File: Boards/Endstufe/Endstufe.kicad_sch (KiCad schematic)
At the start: 59 parts, among them J1 HV In, J10 240V VU, J2 Relais, J3 Audio_In, J4 Übertrager, J5 Gegenkopplung, J6 12V out, J7 Conn_01x08, J8 12V In, J9 VU-Meter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

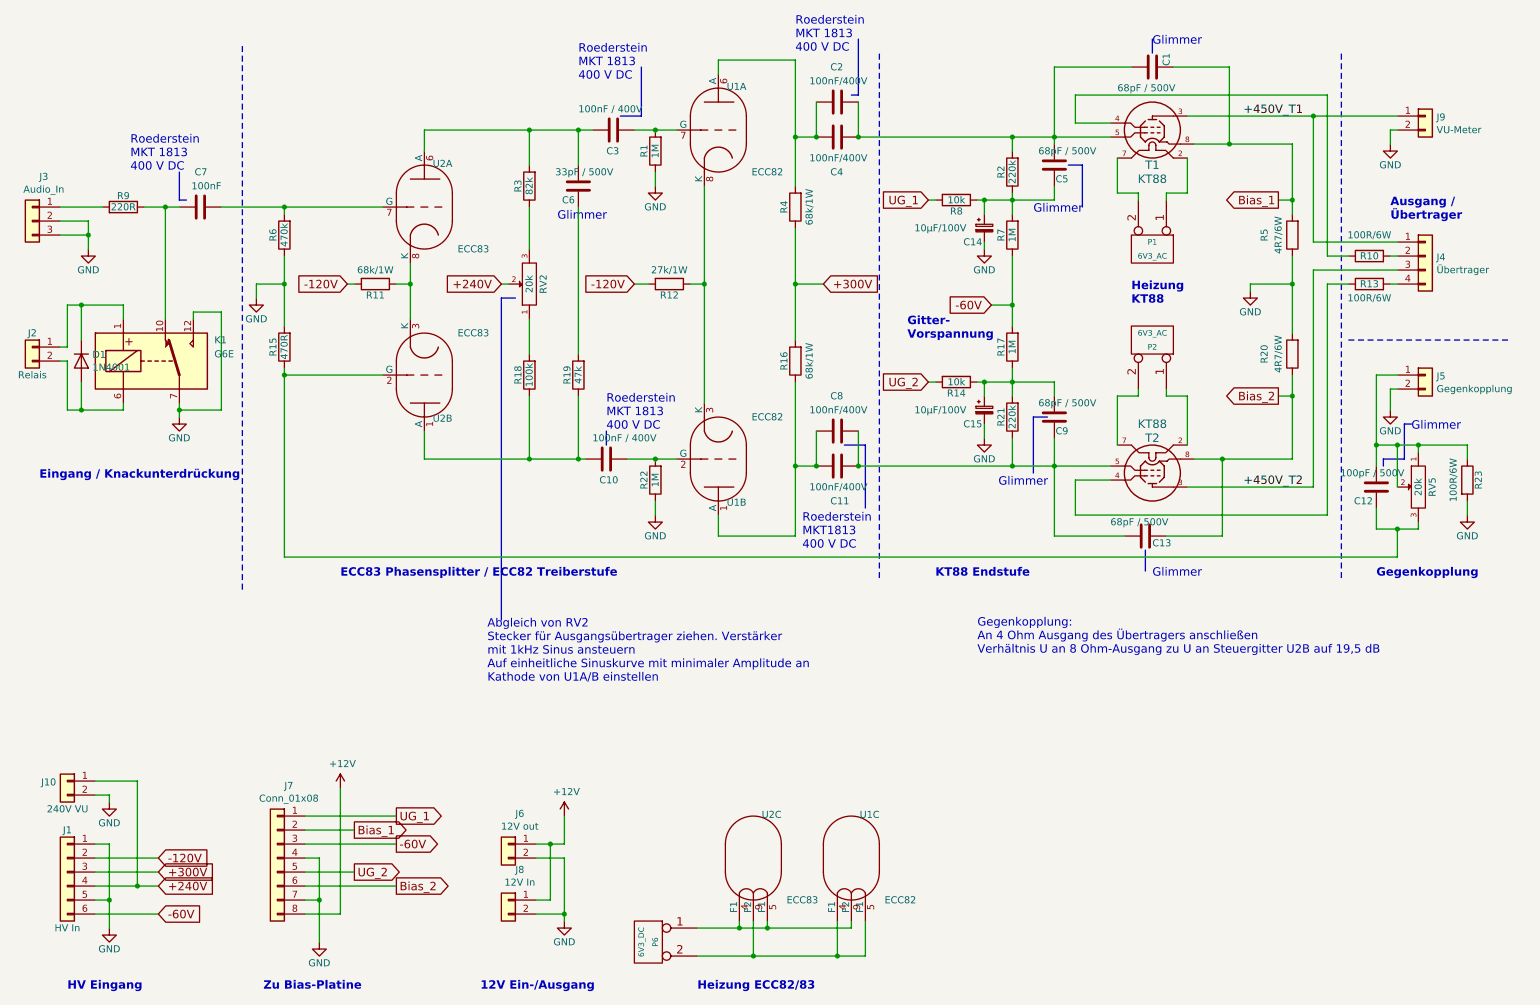
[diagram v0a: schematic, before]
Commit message: 6.3V, 400V und 400V Regler Boards bestellt
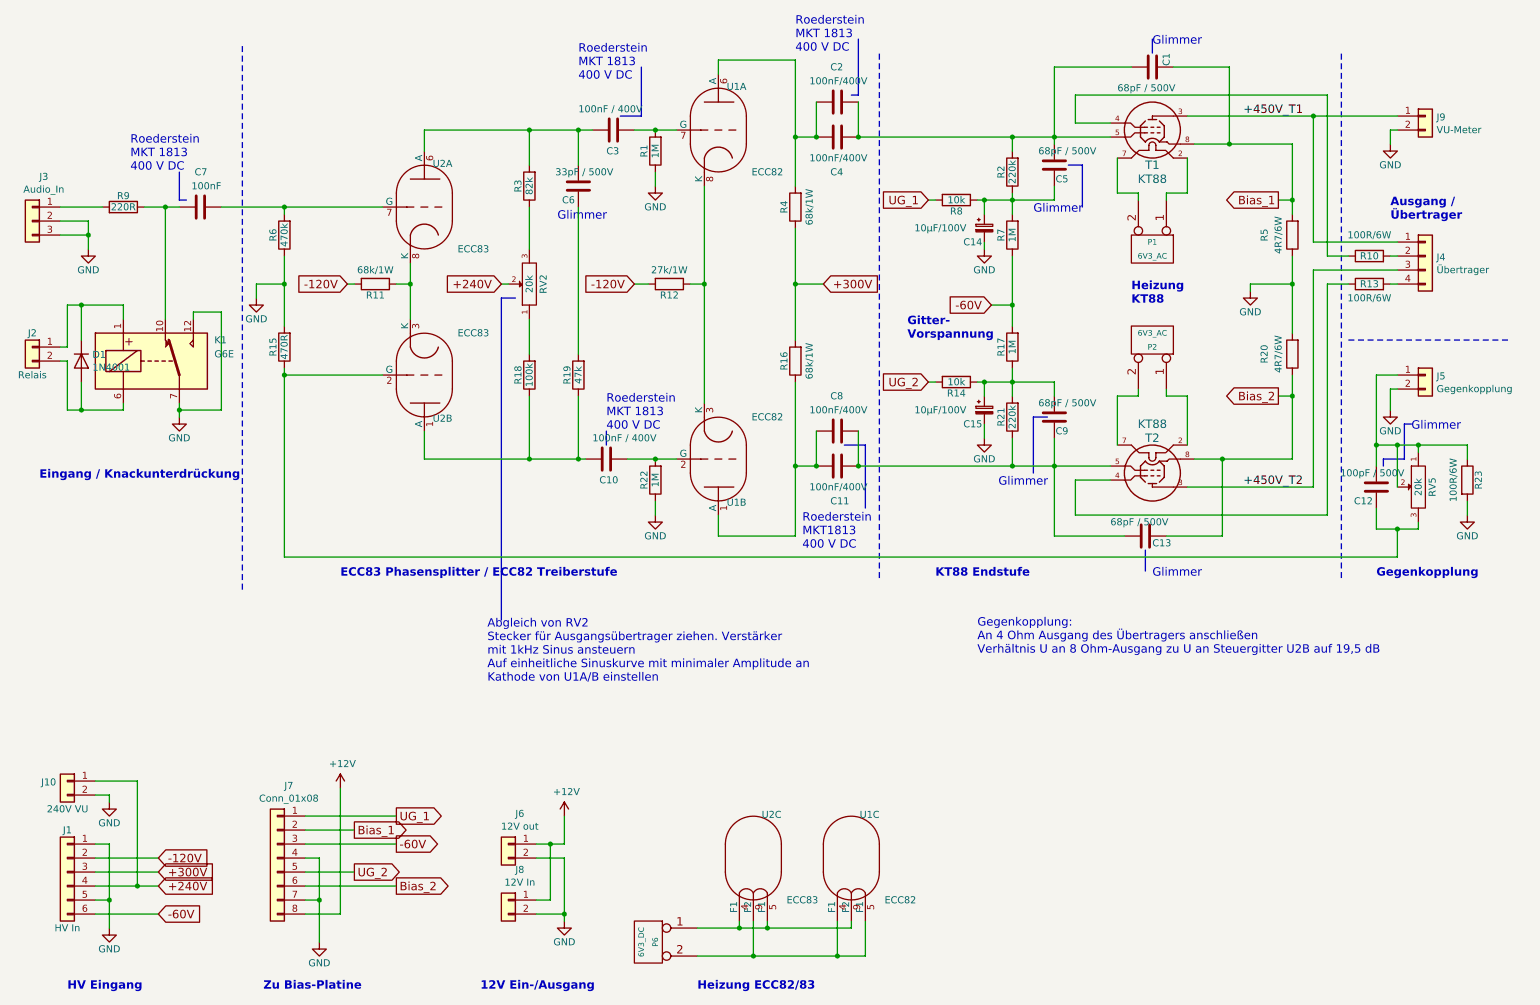
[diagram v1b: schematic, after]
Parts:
- J7: footprint (none) -> Connector_IDC:IDC-Header_2x04_P2.54mm_Vertical

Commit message: Leiterplatte erstellt
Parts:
- removed K1: G6E, Relay_THT:Relay_SPDT_Omron_G6E, symbol Endstufe-rescue:G6E
- added H1, H2, H3, H4, H5, H6: MountingHole, MountingHole:MountingHole_3.2mm_M3, symbol Mechanical:MountingHole
- added K2: G5V-1, Relay_THT:Relay_SPDT_Omron_G5V-1, symbol Relay:G5V-1
- C1, C12, C13, C5, C9: footprint Capacitor_THT:C_Disc_D7.5mm_W4.4mm_P5.00mm -> Capacitor_THT:C_Disc_D11.0mm_W5.0mm_P7.50mm
- C10, C11, C2, C3, C4, C7, C8: footprint Capacitor_THT:C_Axial_L22.0mm_D9.5mm_P27.50mm_Horizontal -> Capacitor_THT:C_Axial_L19.0mm_D7.5mm_P25.00mm_Horizontal
- C14, C15: value 10µF/100V -> 10µF/400V; footprint Capacitor_THT:CP_Radial_D6.3mm_P2.50mm -> Capacitor_THT:CP_Radial_D12.5mm_P5.00mm
- C6: footprint Capacitor_THT:C_Disc_D6.0mm_W4.4mm_P5.00mm -> Capacitor_THT:C_Disc_D11.0mm_W5.0mm_P7.50mm
- J1: footprint Connector_TE-Connectivity:TE_MATE-N-LOK_1-770875-x_2x03_P4.14mm_Vertical -> Connector_Molex:Molex_Mini-Fit_Jr_5566-06A_2x03_P4.20mm_Vertical
- J10, J5, J9, P1, P2, P6: footprint Connector_TE-Connectivity:TE_MATE-N-LOK_1-770866-x_1x02_P4.14mm_Vertical -> Connector_Molex:Molex_Mini-Fit_Jr_5566-02A_2x01_P4.20mm_Vertical
- J4: footprint Connector_TE-Connectivity:TE_MATE-N-LOK_350211-1_1x04_P5.08mm_Vertical -> Connector_Molex:Molex_Mini-Fit_Jr_5566-04A_2x02_P4.20mm_Vertical
- RV2, RV5: footprint Potentiometer_THT:Potentiometer_Piher_PT-10-V10_Vertical_Hole -> Potentiometer_THT:Potentiometer_Vishay_T7-YA_Single_Vertical
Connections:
- net +240V: now also J1.5 (Pin_5); no longer J1.4 (Pin_4)
- net +300V: now also J1.6 (Pin_6); no longer J1.3 (Pin_3)
- net -120V: now also J1.1 (Pin_1); no longer J1.2 (Pin_2)
- net -60V: now also J1.2 (Pin_2); no longer J1.6 (Pin_6)
- net Bias_2: now also C13.2; no longer C13.1
- net GND: now also C14.1, C15.1, J1.3 (Pin_3), J1.4 (Pin_4), K2.10, K2.5, K2.6; no longer C14.2, C15.2, J1.1 (Pin_1), J1.5 (Pin_5)
- net at C11.1, C8.1, C9.1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: now also C13.1; no longer C13.2
- net at C5.1, R2.1, R7.2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: now also C14.2; no longer C14.1
- net at C9.2, R14.1, R17.1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: now also C15.2; no longer C15.1
- net at C7.1, R9.1: now also K2.1
- net at D1.1 (K), J2.1 (Pin_1): now also K2.2
- net at D1.2 (A), J2.2 (Pin_2): now also K2.9
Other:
- moved on the sheet: C13
